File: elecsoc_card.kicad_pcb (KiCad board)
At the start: 2 copper layers, 88 x 50 mm, 23 parts, among them J1 Conn_01x02_Pin, U1 NA555D

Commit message: New PCB design
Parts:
- added C3: 10u, Capacitor_SMD:C_0805_2012Metric_Pad1.18x1.45mm_HandSolder, F.Cu at (154.2, 65.5)
- added J2: Conn_01x02_Pin, Connector_PinHeader_2.54mm:PinHeader_2x01_P2.54mm_Vertical, F.Cu at (103.5, 72.6)
- added R12: 1k, Resistor_SMD:R_0805_2012Metric_Pad1.20x1.40mm_HandSolder, F.Cu at (103.4, 82.0)
- added R13: 5k, Resistor_SMD:R_0805_2012Metric_Pad1.20x1.40mm_HandSolder, F.Cu at (120.6, 96.4)
- added R14: 5k, Resistor_SMD:R_1206_3216Metric, F.Cu at (106.8, 96.3)
- added R15: 5k, Resistor_SMD:R_0805_2012Metric_Pad1.20x1.40mm_HandSolder, F.Cu at (113.8, 96.4)
- added R16: 5k, Resistor_SMD:R_0603_1608Metric, F.Cu at (127.5, 96.4)
- added R17: 5k, Resistor_SMD:R_0402_1005Metric, F.Cu at (133.8, 96.4)
- added R18: 80k, Resistor_SMD:R_0805_2012Metric_Pad1.20x1.40mm_HandSolder, F.Cu at (159.0, 56.9)
- added R19: 80k, Resistor_SMD:R_0805_2012Metric_Pad1.20x1.40mm_HandSolder, F.Cu at (156.8, 56.9)
- R1, R2: value 50k -> 80k
- R3, R4, R5, R6, R7: value 390 -> 3k
- moved C1 19.9 mm to (149.9, 65.5)
- moved R1 19.2 mm to (150.2, 56.9), turned to 90 degrees
- moved R2 18.9 mm to (153.0, 56.9)
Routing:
- net GND: track 73.4 -> 136.6 mm, vias 2 -> 3
- net Net-(R12-Pad2): track 0.00 -> 40.7 mm
- net Net-(U1-THR): track 10.6 -> 35.5 mm, vias 0 -> 2
- net Net-(U1-DIS): track 5.73 -> 29.4 mm, vias 0 -> 2
- net +5V: track 65.3 -> 79.9 mm
- net +5V_PinHeaders: track 0.00 -> 12.5 mm
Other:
- board text added: "0.52s"
- board text added: "0402"
- board text added: "0603"
- board text added: "0805"
- board text added: "1206"
- board text added: "2.08s"
- board text added: "C"
- board text added: "R"

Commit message: Updated PCB
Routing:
- net GND: track 136.6 -> 141.0 mm
- net Net-(U1-THR): track 35.5 -> 34.8 mm
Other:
- board text removed: "0.52s"
- board text removed: "2.08s"
- board text removed: "C"
- board text removed: "R"

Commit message: Components placed and routed
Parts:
- added R20: 1k, Resistor_SMD:R_0402_1005Metric, F.Cu at (120.0, 97.4)
- added R21: 1k, Resistor_SMD:R_0402_1005Metric, F.Cu at (121.5, 97.4)
- R1, R18, R19, R2: value 80k -> 78k7; footprint Resistor_SMD:R_0805_2012Metric_Pad1.20x1.40mm_HandSolder -> Resistor_SMD:R_1206_3216Metric
- R10, R8, R9: footprint Resistor_SMD:R_0805_2012Metric_Pad1.20x1.40mm_HandSolder -> Resistor_SMD:R_0603_1608Metric
- R11, R3, R4, R5, R6, R7: footprint Resistor_SMD:R_0805_2012Metric_Pad1.20x1.40mm_HandSolder -> Resistor_SMD:R_1206_3216Metric
- R12: value 1k -> 150; footprint Resistor_SMD:R_0805_2012Metric_Pad1.20x1.40mm_HandSolder -> Resistor_SMD:R_0603_1608Metric
- R13, R15: value 5k -> 150; footprint Resistor_SMD:R_0805_2012Metric_Pad1.20x1.40mm_HandSolder -> Resistor_SMD:R_0603_1608Metric
- R14: value 5k -> 150; footprint Resistor_SMD:R_1206_3216Metric -> Resistor_SMD:R_0603_1608Metric
- R16: value 5k -> 1k; footprint Resistor_SMD:R_0603_1608Metric -> Resistor_SMD:R_0402_1005Metric
- R17: value 5k -> 1k
- moved R17 13.9 mm to (120.0, 95.1)
- moved R13 13.6 mm to (107.0, 97.1)
- moved R12 11.7 mm to (105.0, 93.6)
- moved R16 9.06 mm to (118.5, 97.4)
- moved R15 8.83 mm to (105.0, 97.1)
- moved R14 3.79 mm to (103.1, 97.1)
- moved R11 0.40 mm to (164.0, 61.1)
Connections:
- J2 pad 1: +5V_PinHeaders -> +5V
- R12 pad 1: +5V_PinHeaders -> +5V
- R16 pad 1: Net-(R12-Pad2) -> Net-(R16-Pad1)
- R17 pad 1: Net-(R12-Pad2) -> +5V
- R17 pad 2: GND -> Net-(R16-Pad1)
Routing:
- net +5V: track 79.9 -> 125.8 mm
- net Net-(R12-Pad2): track 40.7 -> 5.78 mm
- net +5V_PinHeaders: track 12.1 -> 0.00 mm
- net GND: track 141.0 -> 151.9 mm, vias 3 -> 4
- net Net-(R16-Pad1): track 0.00 -> 4.28 mm
- net Net-(J1-Pin_1): track 8.10 -> 7.54 mm
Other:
- board text removed: "0402"
- board text removed: "0603"
- board text removed: "0805"
- board text removed: "1206"

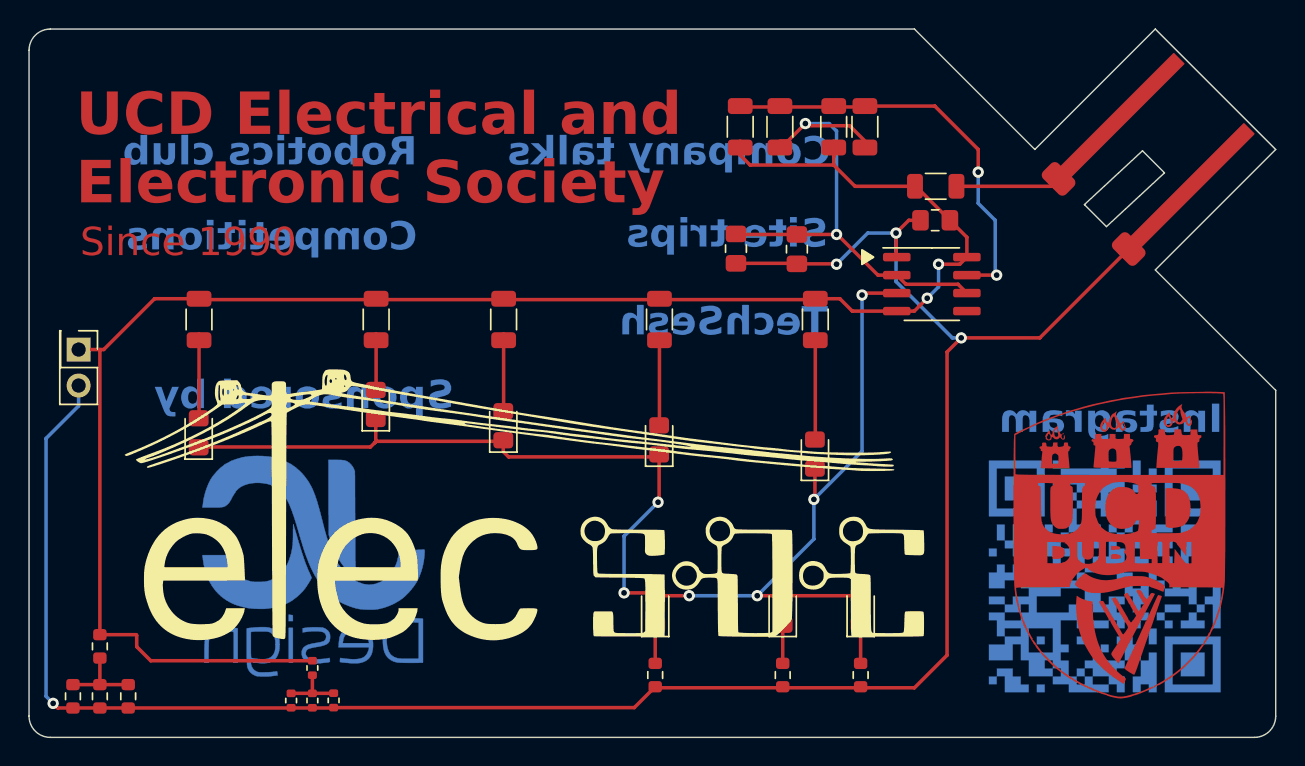
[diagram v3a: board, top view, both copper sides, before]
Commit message: Silkscreen added
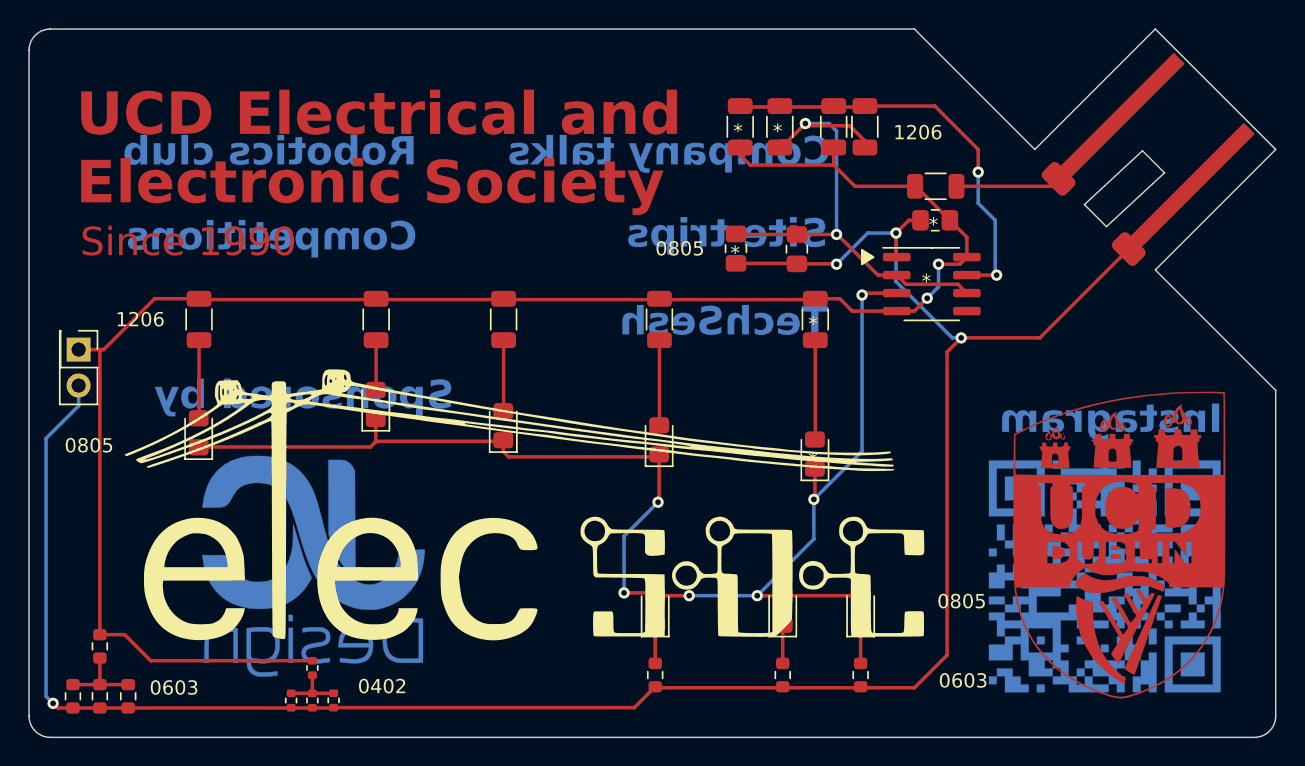
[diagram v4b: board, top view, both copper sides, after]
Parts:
- renumbered D4 to D1, D5 to D2, D2 to D4, D1 to D5, R6 to R3, R7 to R4, R4 to R6, R3 to R7
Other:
- board text added: "*"
- board text added: "0402"
- board text added: "0603"
- board text added: "0805"
- board text added: "1206"
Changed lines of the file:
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@@
 		(descr "Resistor SMD 1206 (3216 Metric), square (rectangular) end terminal, IPC_7351 nominal, (Body size source: IPC-SM-782 page 72, https://www.pcb-3d.com/wordpress/wp-content/uploads/ipc-sm-782a_amendment_1_and_2.pdf), generated with kicad-footprint-generator")
 		(tags "resistor")
-		(property "Reference" "R6"
+		(property "Reference" "R3"
 			(at 0 -1.82 90)
 			(layer "F.SilkS")
@@
 		(descr "Resistor SMD 1206 (3216 Metric), square (rectangular) end terminal, IPC_7351 nominal, (Body size source: IPC-SM-782 page 72, https://www.pcb-3d.com/wordpress/wp-content/uploads/ipc-sm-782a_amendment_1_and_2.pdf), generated with kicad-footprint-generator")
 		(tags "resistor")
-		(property "Reference" "R7"
+		(property "Reference" "R4"
 			(at 0 -1.82 90)
 			(layer "F.SilkS")
@@
 		(descr "LED SMD 0805 (2012 Metric), square (rectangular) end terminal, IPC_7351 nominal, (Body size source: https://docs.google.com/spreadsheets/d/1BsfQQcO9C6DZCsRaXUlFlo91Tg2WpOkGARC1WS5S8t0/edit?usp=sharing), generated with kicad-footprint-generator")
 		(tags "LED handsolder")
-		(property "Reference" "D4"
+		(property "Reference" "D1"
 			(at -2 -1.975 180)
 			(layer "F.SilkS")
@@
 		(descr "Resistor SMD 1206 (3216 Metric), square (rectangular) end terminal, IPC_7351 nominal, (Body size source: IPC-SM-782 page 72, https://www.pcb-3d.com/wordpress/wp-content/uploads/ipc-sm-782a_amendment_1_and_2.pdf), generated with kicad-footprint-generator")
 		(tags "resistor")
-		(property "Reference" "R4"
+		(property "Reference" "R6"
 			(at 0 -1.82 90)
 			(layer "F.SilkS")
@@
 		(descr "LED SMD 0805 (2012 Metric), square (rectangular) end terminal, IPC_7351 nominal, (Body size source: https://docs.google.com/spreadsheets/d/1BsfQQcO9C6DZCsRaXUlFlo91Tg2WpOkGARC1WS5S8t0/edit?usp=sharing), generated with kicad-footprint-generator")
 		(tags "LED handsolder")
-		(property "Reference" "D5"
+		(property "Reference" "D2"
 			(at -3 0.025 180)
 			(layer "F.SilkS")
@@
 		(descr "Resistor SMD 1206 (3216 Metric), square (rectangular) end terminal, IPC_7351 nominal, (Body size source: IPC-SM-782 page 72, https://www.pcb-3d.com/wordpress/wp-content/uploads/ipc-sm-782a_amendment_1_and_2.pdf), generated with kicad-footprint-generator")
 		(tags "resistor")
-		(property "Reference" "R3"
+		(property "Reference" "R7"
 			(at 0 -1.82 90)
 			(layer "F.SilkS")
@@
 		(descr "LED SMD 0805 (2012 Metric), square (rectangular) end terminal, IPC_7351 nominal, (Body size source: https://docs.google.com/spreadsheets/d/1BsfQQcO9C6DZCsRaXUlFlo91Tg2WpOkGARC1WS5S8t0/edit?usp=sharing), generated with kicad-footprint-generator")
 		(tags "LED handsolder")
-		(property "Reference" "D2"
+		(property "Reference" "D4"
 			(at -3 0.025 180)
 			(layer "F.SilkS")
@@
 		(descr "LED SMD 0805 (2012 Metric), square (rectangular) end terminal, IPC_7351 nominal, (Body size source: https://docs.google.com/spreadsheets/d/1BsfQQcO9C6DZCsRaXUlFlo91Tg2WpOkGARC1WS5S8t0/edit?usp=sharing), generated with kicad-footprint-generator")
 		(tags "LED handsolder")
-		(property "Reference" "D1"
+		(property "Reference" "D5"
 			(at -2.5 2.025 180)
 			(layer "F.SilkS")
@@
 		)
 	)
+	(gr_text "*"
+		(at 152.5 57.8 0)
+		(layer "F.SilkS")
+		(effects
+			(font
+				(size 1 1)
+				(thickness 0.16)
+			)
+			(justify left bottom)
+		)
+	)
+	(gr_text "0805"
+		(at 164.1 91 0)
+		(layer "F.SilkS")
+		(effects
+			(font
+				(size 1 1)
+				(thickness 0.16)
+			)
+			(justify left bottom)
+		)
+	)
+	(gr_text "1206"
+		(at 161 57.9 0)
+		(layer "F.SilkS")
+		(effects
+			(font
+				(size 1 1)
+				(thickness 0.16)
+			)
+			(justify left bottom)
+		)
+	)
+	(gr_text "0402"
+		(at 123.2 97 0)
+		(layer "F.SilkS")
+		(effects
+			(font
+				(size 1 1)
+				(thickness 0.16)
+			)
+			(justify left bottom)
+		)
+	)
+	(gr_text "*"
+		(at 155 81 0)
+		(layer "F.SilkS")
+		(effects
+			(font
+				(size 1 1)
+				(thickness 0.16)
+			)
+			(justify left bottom)
+		)
+	)
+	(gr_text "1206"
+		(at 106.1 71.1 0)
+		(layer "F.SilkS")
+		(effects
+			(font
+				(size 1 1)
+				(thickness 0.16)
+			)
+			(justify left bottom)
+		)
+	)
+	(gr_text "*"
+		(at 155 71.4 0)
+		(layer "F.SilkS")
+		(effects
+			(font
+				(size 1 1)
+				(thickness 0.16)
+			)
+			(justify left bottom)
+		)
+	)
+	(gr_text "*"
+		(at 149.7 57.8 0)
+		(layer "F.SilkS")
+		(effects
+			(font
+				(size 1 1)
+				(thickness 0.16)
+			)
+			(justify left bottom)
+		)
+	)
+	(gr_text "0603"
+		(at 108.5 97.1 0)
+		(layer "F.SilkS")
+		(effects
+			(font
+				(size 1 1)
+				(thickness 0.16)
+			)
+			(justify left bottom)
+		)
+	)
+	(gr_text "*"
+		(at 149.5 66.4 0)
+		(layer "F.SilkS")
+		(effects
+			(font
+				(size 1 1)
+				(thickness 0.16)
+			)
+			(justify left bottom)
+		)
+	)
+	(gr_text "0805"
+		(at 102.5 80 0)
+		(layer "F.SilkS")
+		(effects
+			(font
+				(size 1 1)
+				(thickness 0.16)
+			)
+			(justify left bottom)
+		)
+	)
+	(gr_text "*"
+		(at 163 68.4 0)
+		(layer "F.SilkS")
+		(effects
+			(font
+				(size 1 1)
+				(thickness 0.16)
+			)
+			(justify left bottom)
+		)
+	)
+	(gr_text "*"
+		(at 163.5 64.4 0)
+		(layer "F.SilkS")
+		(effects
+			(font
+				(size 1 1)
+				(thickness 0.16)
+			)
+			(justify left bottom)
+		)
+	)
+	(gr_text "0805"
+		(at 144.2 66.1 0)
+		(layer "F.SilkS")
+		(effects
+			(font
+				(size 1 1)
+				(thickness 0.16)
+			)
+			(justify left bottom)
+		)
+	)
+	(gr_text "0603"
+		(at 164.2 96.6 0)
+		(layer "F.SilkS")
+		(effects
+			(font
+				(size 1 1)
+				(thickness 0.16)
+			)
+			(justify left bottom)
+		)
+	)
 	(gr_text "Company talks"
 		(at 156.6 59.8 0)
@@
 	)
 	(segment
-		(start 107.55 92.75)
-		(end 105 92.75)
+		(start 120 94.59)
+		(end 108.59 94.59)
 		(width 0.25)
 		(layer "F.Cu")
@@
 	)
 	(segment
-		(start 165 63.5)
-		(end 162.6 61.1)
+		(start 106.75 92.75)
+		(end 105 92.75)
 		(width 0.25)
 		(layer "F.Cu")
@@
 	)
 	(segment
-		(start 120 94.59)
-		(end 108.59 94.59)
+		(start 165 63.5)
+		(end 162.6 61.1)
 		(width 0.25)
 		(layer "F.Cu")
@@
 	)
 	(segment
-		(start 107.6 93.6)
-		(end 107.6 92.8)
+		(start 108.59 94.59)
+		(end 106.75 92.75)
 		(width 0.25)
 		(layer "F.Cu")
@@
 	)
 	(segment
-		(start 107.6 92.8)
-		(end 107.55 92.75)
-		(width 0.25)
-		(layer "F.Cu")
-		(net 12)
-	)
-	(segment
 		(start 105 72.625)
 		(end 105.275 72.625)
@@
 		(width 0.25)
 		(layer "F.Cu")
-		(net 12)
-	)
-	(segment
-		(start 108.59 94.59)
-		(end 107.6 93.6)
-		(width 0.25)
-		(layer "F.Cu")

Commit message: PCB finished plus gerbers
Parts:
- moved R18 0.60 mm to (159.6, 56.9)
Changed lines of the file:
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@@
 		(allow_soldermask_bridges_in_footprints no)
 		(pcbplotparams
-			(layerselection 0x00010fc_ffffffff)
+			(layerselection 0x00010ff_ffffffff)
 			(plot_on_all_layers_selection 0x0000000_00000000)
 			(disableapertmacros no)
@@
 			(drillshape 0)
 			(scaleselection 1)
-			(outputdirectory "ManufactureFiles/")
+			(outputdirectory "gerber/")
 		)
 	)
@@
 	(footprint "Resistor_SMD:R_1206_3216Metric"
 		(layer "F.Cu")
-		(at 159 56.9 -90)
+		(at 159.6 56.9 -90)
 		(descr "Resistor SMD 1206 (3216 Metric), square (rectangular) end terminal, IPC_7351 nominal, (Body size source: IPC-SM-782 page 72, https://www.pcb-3d.com/wordpress/wp-content/uploads/ipc-sm-782a_amendment_1_and_2.pdf), generated with kicad-footprint-generator")
 		(tags "resistor")
